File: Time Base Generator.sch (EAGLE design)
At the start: 8 parts, among them IC1 4060N, IC2 4013N, X1_32768 CRYSTALS-NOGND-WATCH-3X8

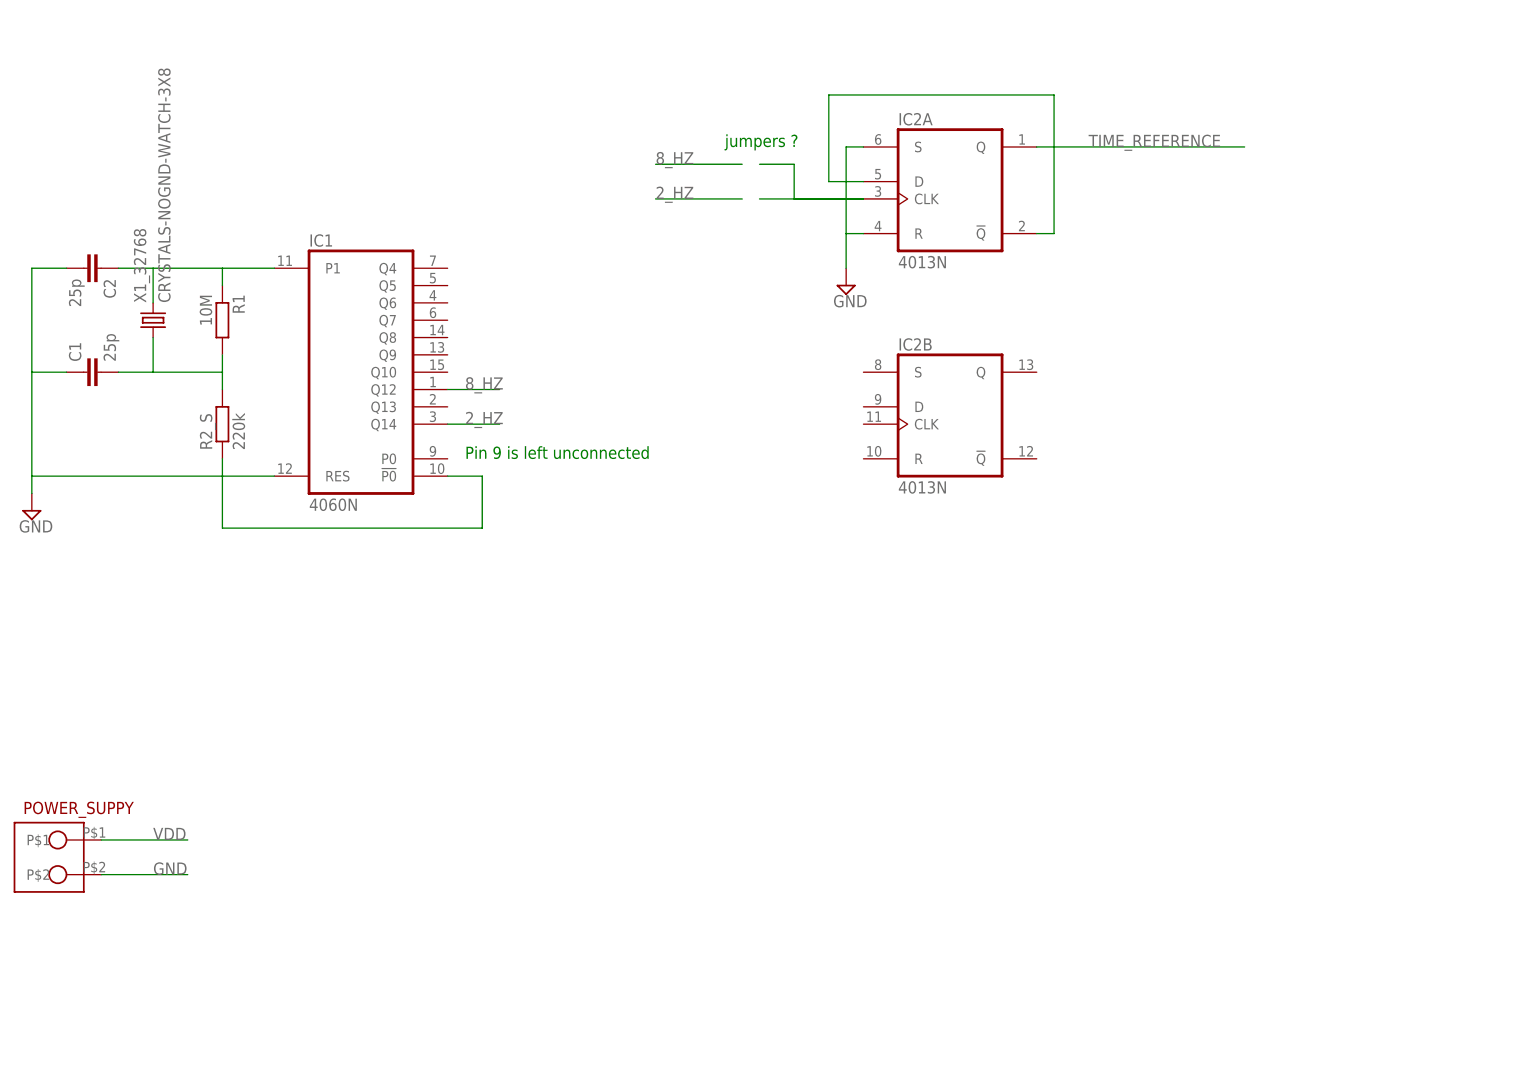
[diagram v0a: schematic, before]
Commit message: Add TubeAlt, rename Control Logic, use jumper
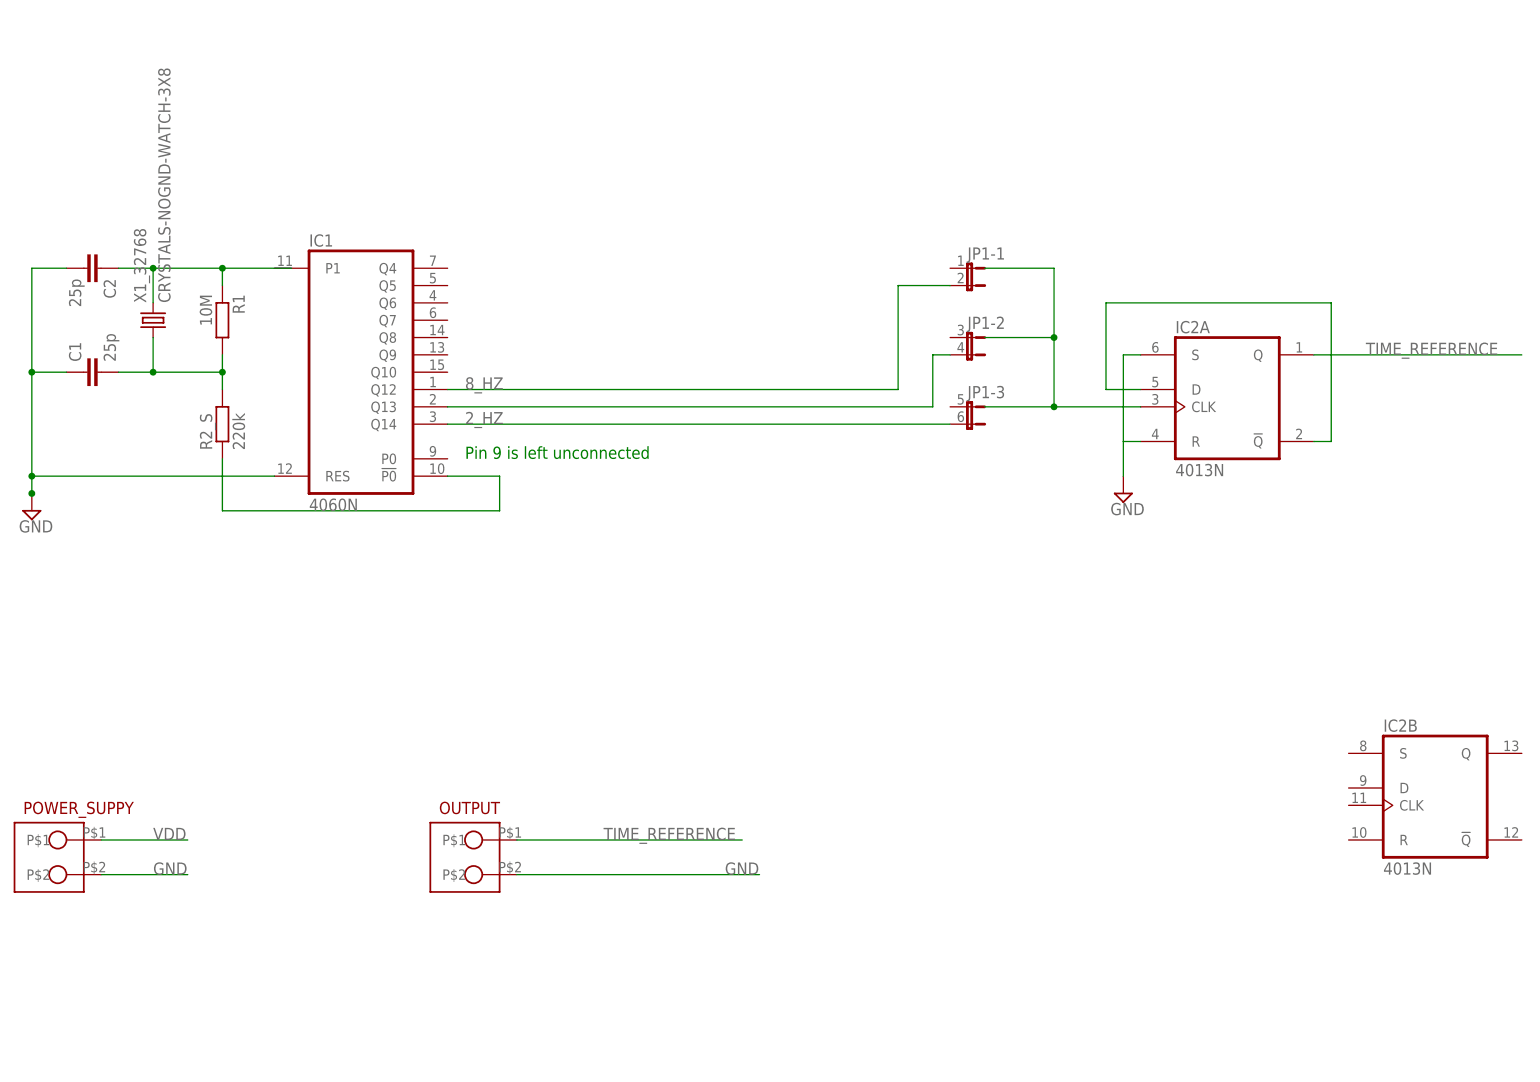
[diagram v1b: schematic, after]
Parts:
- added JP1: (no value), jumper:JP3QE
- added OUTPUT: CON_2_SIL, PGT:CON_2_SIL
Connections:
- new net N$6: IC1A.Q13, JP1-2.2
- net 2_HZ: now also JP1-3.2
- net 8_HZ: now also JP1-1.2
- net GND: now also OUTPUT.P$2
- net N$1: no longer IC1A.P1
- net TIME_REFERENCE: now also OUTPUT.P$1
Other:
- note removed: "jumpers ?"
- moved on the sheet: IC2A, IC2B

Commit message: Separate board for time reference generator
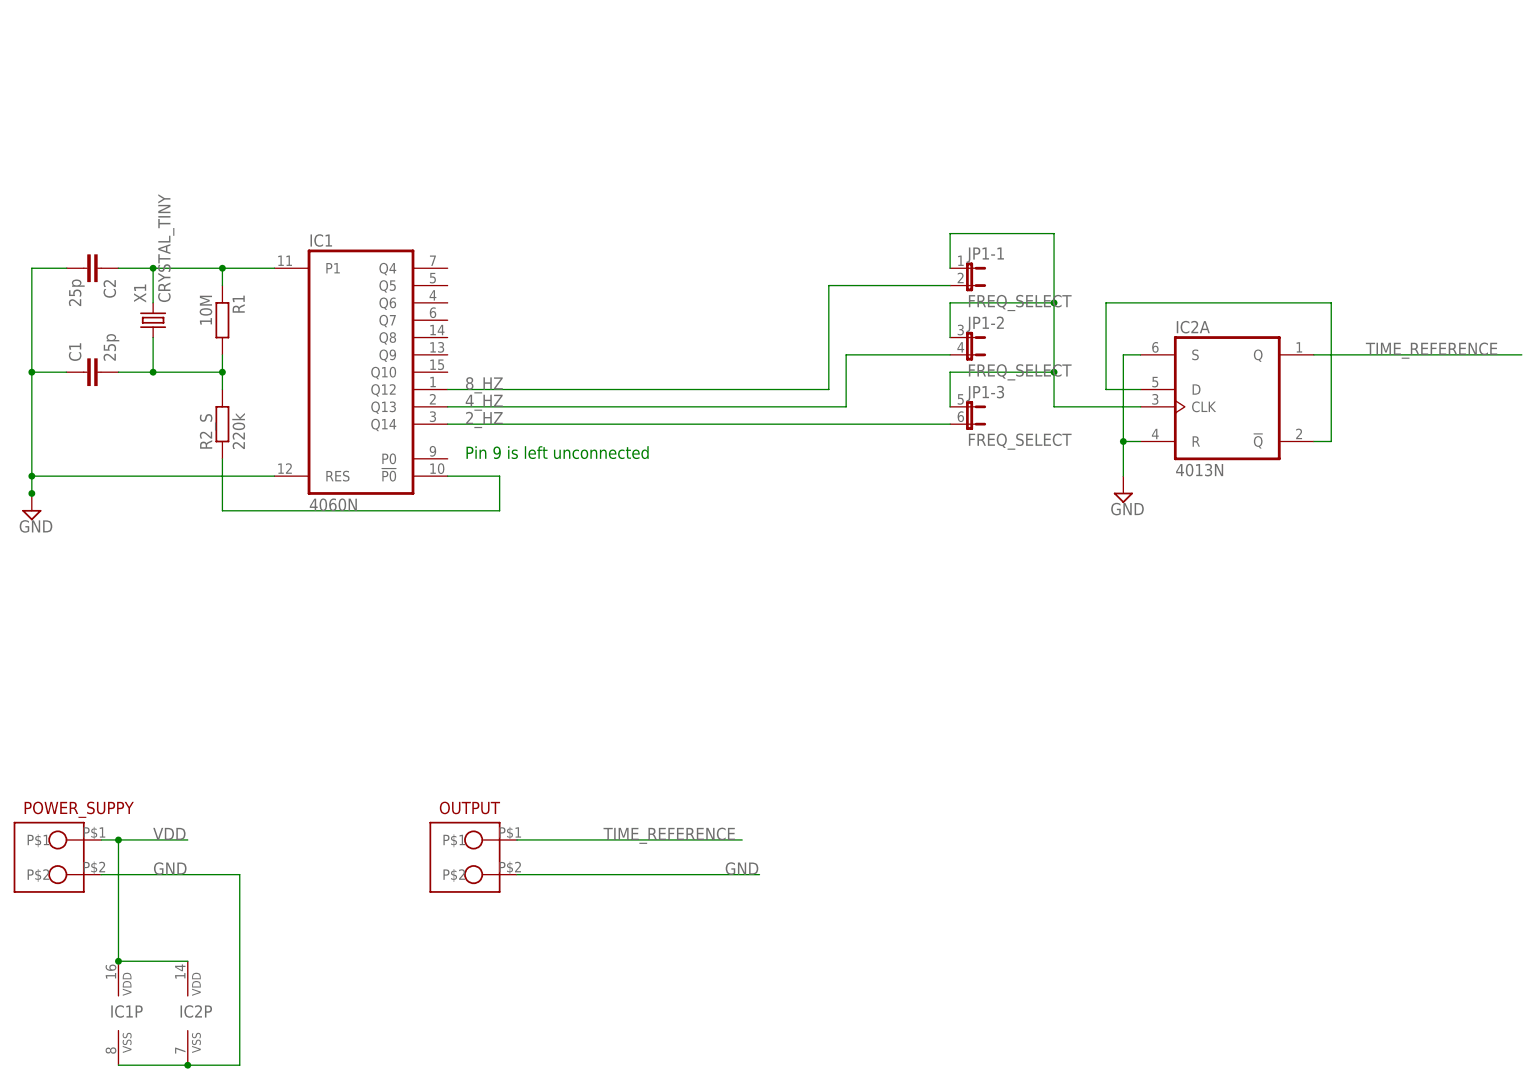
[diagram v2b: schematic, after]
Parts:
- removed X1_32768: CRYSTALS-NOGND-WATCH-3X8, IQD-Frequency-Products:CRYSTALS-NOGND-WATCH-3X8
- added X1: CRYSTAL_TINY, PGT:CRYSTAL_TINY
- JP1: value (none) -> FREQ_SELECT
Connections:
- net N$6 renamed 4_HZ
- removed net N$4: IC2A.CLK
- new net N$8: IC2A.CLK, JP1-1.1, JP1-2.1, JP1-3.1
- net GND: now also IC1P.VSS, IC2P.VSS
- net N$1: now also IC1A.P1, X1.2; no longer X1_32768.2
- net N$2: now also X1.1; no longer X1_32768.1
- net VDD: now also IC1P.VDD, IC2P.VDD
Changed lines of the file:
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@@
 <part name="C1" library="resistor" deviceset="C-EU" device="050-025X075" value="25p"/>
 <part name="C2" library="resistor" deviceset="C-EU" device="050-025X075" value="25p"/>
-<part name="X1_32768" library="IQD-Frequency-Products" deviceset="CRYSTALS-NOGND" device="-WATCH-3X8"/>
 <part name="IC2" library="40xx" deviceset="4013" device="N"/>
 <part name="SUPPLY1" library="supply2" deviceset="GND" device=""/>
@@
 <part name="SUPPLY2" library="supply2" deviceset="GND" device=""/>
 <part name="OUTPUT" library="PGT" deviceset="CON_2_SIL" device=""/>
-<part name="JP1" library="jumper" deviceset="JP3QE" device=""/>
+<part name="JP1" library="jumper" deviceset="JP3QE" device="" value="FREQ_SELECT"/>
+<part name="X1" library="PGT" deviceset="CRYSTAL_TINY" device=""/>
 </parts>
 <sheets>
@@
 <instance part="C1" gate="G$1" x="43.18" y="208.28" rot="R90"/>
 <instance part="C2" gate="G$1" x="45.72" y="223.52" rot="R270"/>
-<instance part="X1_32768" gate="G$1" x="53.34" y="215.9" rot="R90"/>
 <instance part="IC2" gate="A" x="210.82" y="203.2"/>
-<instance part="IC2" gate="B" x="241.3" y="144.78"/>
 <instance part="SUPPLY1" gate="GND" x="35.56" y="187.96"/>
 <instance part="POWER_SUPPY" gate="G$1" x="38.1" y="137.16"/>
@@
 <instance part="JP1" gate="-2" x="172.72" y="213.36" rot="R270"/>
 <instance part="JP1" gate="-3" x="172.72" y="203.2" rot="R270"/>
+<instance part="IC1" gate="P" x="48.26" y="114.3"/>
+<instance part="IC2" gate="P" x="58.42" y="114.3"/>
+<instance part="X1" gate="G$1" x="53.34" y="215.9" rot="R90"/>
 </instances>
 <busses>
@@
 <segment>
 <pinref part="POWER_SUPPY" gate="G$1" pin="P$2"/>
-<wire x1="45.72" y1="134.62" x2="58.42" y2="134.62" width="0.1524" layer="91"/>
+<wire x1="45.72" y1="134.62" x2="66.04" y2="134.62" width="0.1524" layer="91"/>
 <label x="53.34" y="134.62" size="1.778" layer="95"/>
-</segment>
-<segment>
-<pinref part="IC2" gate="A" pin="R"/>
-<pinref part="IC2" gate="A" pin="S"/>
-<wire x1="198.12" y1="210.82" x2="195.58" y2="210.82" width="0.1524" layer="91"/>
-<wire x1="195.58" y1="210.82" x2="195.58" y2="198.12" width="0.1524" layer="91"/>
-<wire x1="195.58" y1="198.12" x2="198.12" y2="198.12" width="0.1524" layer="91"/>
-<pinref part="SUPPLY2" gate="GND" pin="GND"/>
-<wire x1="195.58" y1="193.04" x2="195.58" y2="198.12" width="0.1524" layer="91"/>
+<wire x1="66.04" y1="106.68" x2="66.04" y2="134.62" width="0.1524" layer="91"/>
+<pinref part="IC2" gate="P" pin="VSS"/>
+<wire x1="58.42" y1="106.68" x2="66.04" y2="106.68" width="0.1524" layer="91"/>
+<pinref part="IC1" gate="P" pin="VSS"/>
+<wire x1="48.26" y1="106.68" x2="58.42" y2="106.68" width="0.1524" layer="91"/>
+<junction x="58.42" y="106.68"/>
 </segment>
 <segment>
@@
 <label x="137.16" y="134.62" size="1.778" layer="95"/>
 </segment>
+<segment>
+<pinref part="IC2" gate="A" pin="S"/>
+<pinref part="SUPPLY2" gate="GND" pin="GND"/>
+<wire x1="198.12" y1="210.82" x2="195.58" y2="210.82" width="0.1524" layer="91"/>
+<wire x1="195.58" y1="210.82" x2="195.58" y2="198.12" width="0.1524" layer="91"/>
+<pinref part="IC2" gate="A" pin="R"/>
+<wire x1="195.58" y1="198.12" x2="195.58" y2="193.04" width="0.1524" layer="91"/>
+<wire x1="198.12" y1="198.12" x2="195.58" y2="198.12" width="0.1524" layer="91"/>
+<junction x="195.58" y="198.12"/>
+</segment>
 </net>
 <net name="VDD" class="0">
 <segment>
 <pinref part="POWER_SUPPY" gate="G$1" pin="P$1"/>
-<wire x1="45.72" y1="139.7" x2="58.42" y2="139.7" width="0.1524" layer="91"/>
 <label x="53.34" y="139.7" size="1.778" layer="95"/>
+<wire x1="58.42" y1="139.7" x2="48.26" y2="139.7" width="0.1524" layer="91"/>
+<pinref part="IC1" gate="P" pin="VDD"/>
+<pinref part="IC2" gate="P" pin="VDD"/>
+<wire x1="48.26" y1="139.7" x2="45.72" y2="139.7" width="0.1524" layer="91"/>
+<wire x1="58.42" y1="121.92" x2="48.26" y2="121.92" width="0.1524" layer="91"/>
+<wire x1="48.26" y1="121.92" x2="48.26" y2="139.7" width="0.1524" layer="91"/>
+<junction x="48.26" y="121.92"/>
+<junction x="48.26" y="139.7"/>
 </segment>
 </net>
@@
 <pinref part="IC1" gate="A" pin="Q12"/>
 <label x="99.06" y="205.74" size="1.778" layer="95"/>
-<wire x1="96.52" y1="205.74" x2="162.56" y2="205.74" width="0.1524" layer="91"/>
-<wire x1="162.56" y1="205.74" x2="162.56" y2="220.98" width="0.1524" layer="91"/>
+<wire x1="96.52" y1="205.74" x2="152.4" y2="205.74" width="0.1524" layer="91"/>
+<wire x1="152.4" y1="205.74" x2="152.4" y2="220.98" width="0.1524" layer="91"/>
 <pinref part="JP1" gate="-1" pin="2"/>
-<wire x1="162.56" y1="220.98" x2="170.18" y2="220.98" width="0.1524" layer="91"/>
+<wire x1="152.4" y1="220.98" x2="170.18" y2="220.98" width="0.1524" layer="91"/>
 </segment>
 </net>
@@
 <segment>
 <pinref part="C1" gate="G$1" pin="2"/>
-<pinref part="X1_32768" gate="G$1" pin="1"/>
+<pinref part="R2_S" gate="G$1" pin="2"/>
 <wire x1="48.26" y1="208.28" x2="53.34" y2="208.28" width="0.1524" layer="91"/>
-<wire x1="53.34" y1="208.28" x2="53.34" y2="213.36" width="0.1524" layer="91"/>
-<pinref part="R2_S" gate="G$1" pin="2"/>
 <wire x1="53.34" y1="208.28" x2="63.5" y2="208.28" width="0.1524" layer="91"/>
 <wire x1="63.5" y1="208.28" x2="63.5" y2="205.74" width="0.1524" layer="91"/>
-<junction x="53.34" y="208.28"/>
 <pinref part="R1" gate="G$1" pin="2"/>
 <wire x1="63.5" y1="208.28" x2="63.5" y2="210.82" width="0.1524" layer="91"/>
 <junction x="63.5" y="208.28"/>
+<pinref part="X1" gate="G$1" pin="1"/>
+<wire x1="53.34" y1="213.36" x2="53.34" y2="208.28" width="0.1524" layer="91"/>
+<junction x="53.34" y="208.28"/>
 </segment>
 </net>
@@
 <segment>
 <pinref part="C2" gate="G$1" pin="1"/>
+<pinref part="R1" gate="G$1" pin="1"/>
+<wire x1="48.26" y1="223.52" x2="53.34" y2="223.52" width="0.1524" layer="91"/>
 <wire x1="53.34" y1="223.52" x2="63.5" y2="223.52" width="0.1524" layer="91"/>
-<wire x1="63.5" y1="223.52" x2="73.66" y2="223.52" width="0.1524" layer="91"/>
-<wire x1="53.34" y1="223.52" x2="48.26" y2="223.52" width="0.1524" layer="91"/>
-<pinref part="X1_32768" gate="G$1" pin="2"/>
+<wire x1="63.5" y1="220.98" x2="63.5" y2="223.52" width="0.1524" layer="91"/>
+<pinref part="IC1" gate="A" pin="P1"/>
+<wire x1="63.5" y1="223.52" x2="71.12" y2="223.52" width="0.1524" layer="91"/>
+<junction x="63.5" y="223.52"/>
+<pinref part="X1" gate="G$1" pin="2"/>
 <wire x1="53.34" y1="218.44" x2="53.34" y2="223.52" width="0.1524" layer="91"/>
 <junction x="53.34" y="223.52"/>
-<pinref part="R1" gate="G$1" pin="1"/>
-<wire x1="63.5" y1="220.98" x2="63.5" y2="223.52" width="0.1524" layer="91"/>
-<junction x="63.5" y="223.52"/>
 </segment>
 </net>
@@
 </segment>
 </net>
-<net name="N$6" class="0">
+<net name="4_HZ" class="0">
 <segment>
 <pinref part="IC1" gate="A" pin="Q13"/>
-<wire x1="96.52" y1="203.2" x2="167.64" y2="203.2" width="0.1524" layer="91"/>
-<wire x1="167.64" y1="203.2" x2="167.64" y2="210.82" width="0.1524" layer="91"/>
+<wire x1="96.52" y1="203.2" x2="154.94" y2="203.2" width="0.1524" layer="91"/>
+<wire x1="154.94" y1="203.2" x2="154.94" y2="210.82" width="0.1524" layer="91"/>
 <pinref part="JP1" gate="-2" pin="2"/>
-<wire x1="167.64" y1="210.82" x2="170.18" y2="210.82" width="0.1524" layer="91"/>
+<wire x1="154.94" y1="210.82" x2="170.18" y2="210.82" width="0.1524" layer="91"/>
+<label x="99.06" y="203.2" size="1.778" layer="95"/>
 </segment>
 </net>
@@
 </segment>
 </net>
-<net name="N$4" class="0">
-<segment>
-<wire x1="175.26" y1="203.2" x2="185.42" y2="203.2" width="0.1524" layer="91"/>
-<wire x1="175.26" y1="213.36" x2="185.42" y2="213.36" width="0.1524" layer="91"/>
-<wire x1="185.42" y1="213.36" x2="185.42" y2="203.2" width="0.1524" layer="91"/>
-<wire x1="175.26" y1="223.52" x2="185.42" y2="223.52" width="0.1524" layer="91"/>
-<wire x1="185.42" y1="223.52" x2="185.42" y2="213.36" width="0.1524" layer="91"/>
-<junction x="185.42" y="213.36"/>
-<junction x="185.42" y="203.2"/>
+<net name="N$8" class="0">
+<segment>
+<pinref part="JP1" gate="-3" pin="1"/>
+<wire x1="170.18" y1="203.2" x2="170.18" y2="208.28" width="0.1524" layer="91"/>
+<pinref part="JP1" gate="-2" pin="1"/>
+<wire x1="170.18" y1="213.36" x2="170.18" y2="218.44" width="0.1524" layer="91"/>
+<wire x1="170.18" y1="218.44" x2="185.42" y2="218.44" width="0.1524" layer="91"/>
+<wire x1="185.42" y1="218.44" x2="185.42" y2="208.28" width="0.1524" layer="91"/>
 <pinref part="IC2" gate="A" pin="CLK"/>
+<wire x1="185.42" y1="208.28" x2="185.42" y2="203.2" width="0.1524" layer="91"/>
 <wire x1="185.42" y1="203.2" x2="198.12" y2="203.2" width="0.1524" layer="91"/>
-</segment>
-</net>
+<pinref part="JP1" gate="-1" pin="1"/>
+<wire x1="170.18" y1="223.52" x2="170.18" y2="228.6" width="0.1524" layer="91"/>
+<wire x1="170.18" y1="228.6" x2="185.42" y2="228.6" width="0.1524" layer="91"/>
+<wire x1="185.42" y1="228.6" x2="185.42" y2="218.44" width="0.1524" layer="91"/>
+<junction x="185.42" y="218.44"/>
+<wire x1="170.18" y1="208.28" x2="185.42" y2="208.28" width="0.1524" layer="91"/>
+<junction x="185.42" y="208.28"/>
+</segment>
+</net>
